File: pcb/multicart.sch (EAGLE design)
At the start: 15 parts, among them IC1 74HCT373N, IC2 M27C4001B, IC5 74HCT08N, Q1 BS170

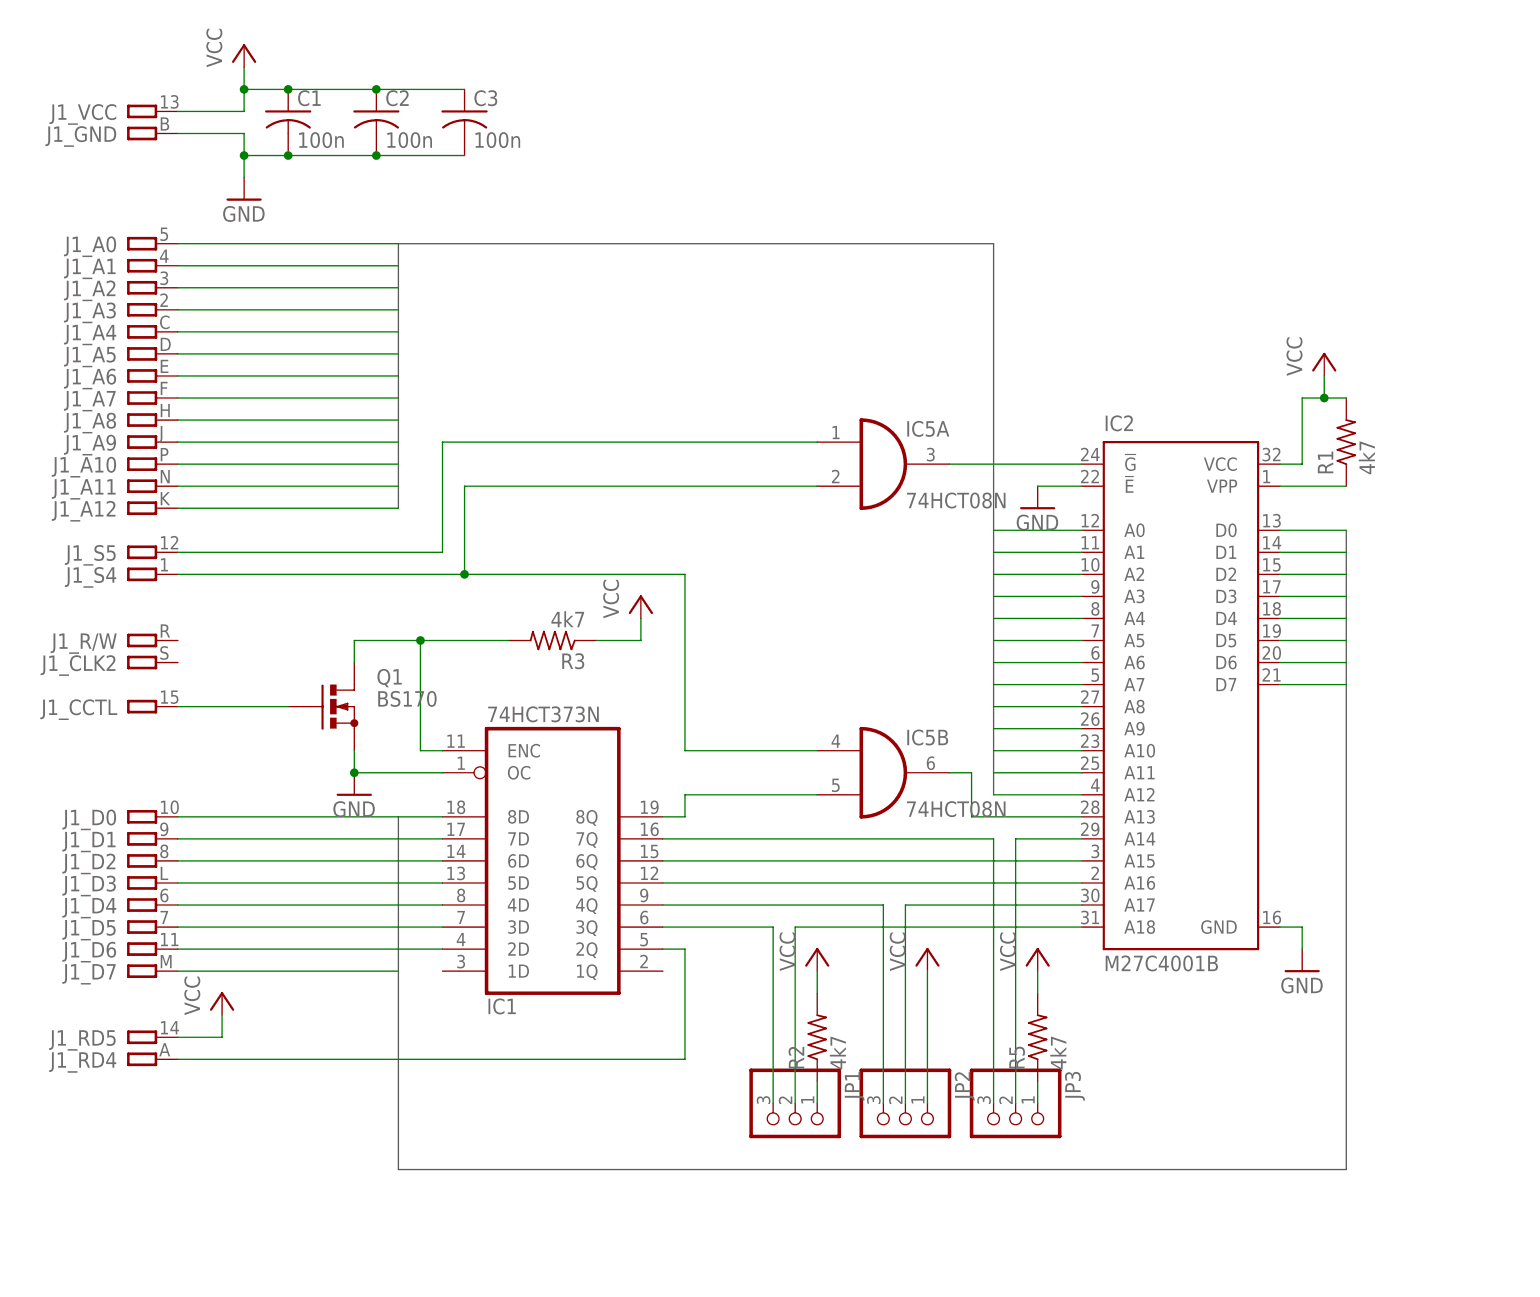
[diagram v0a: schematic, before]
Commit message: Updated the schematic to support 8-mbit flash chips.
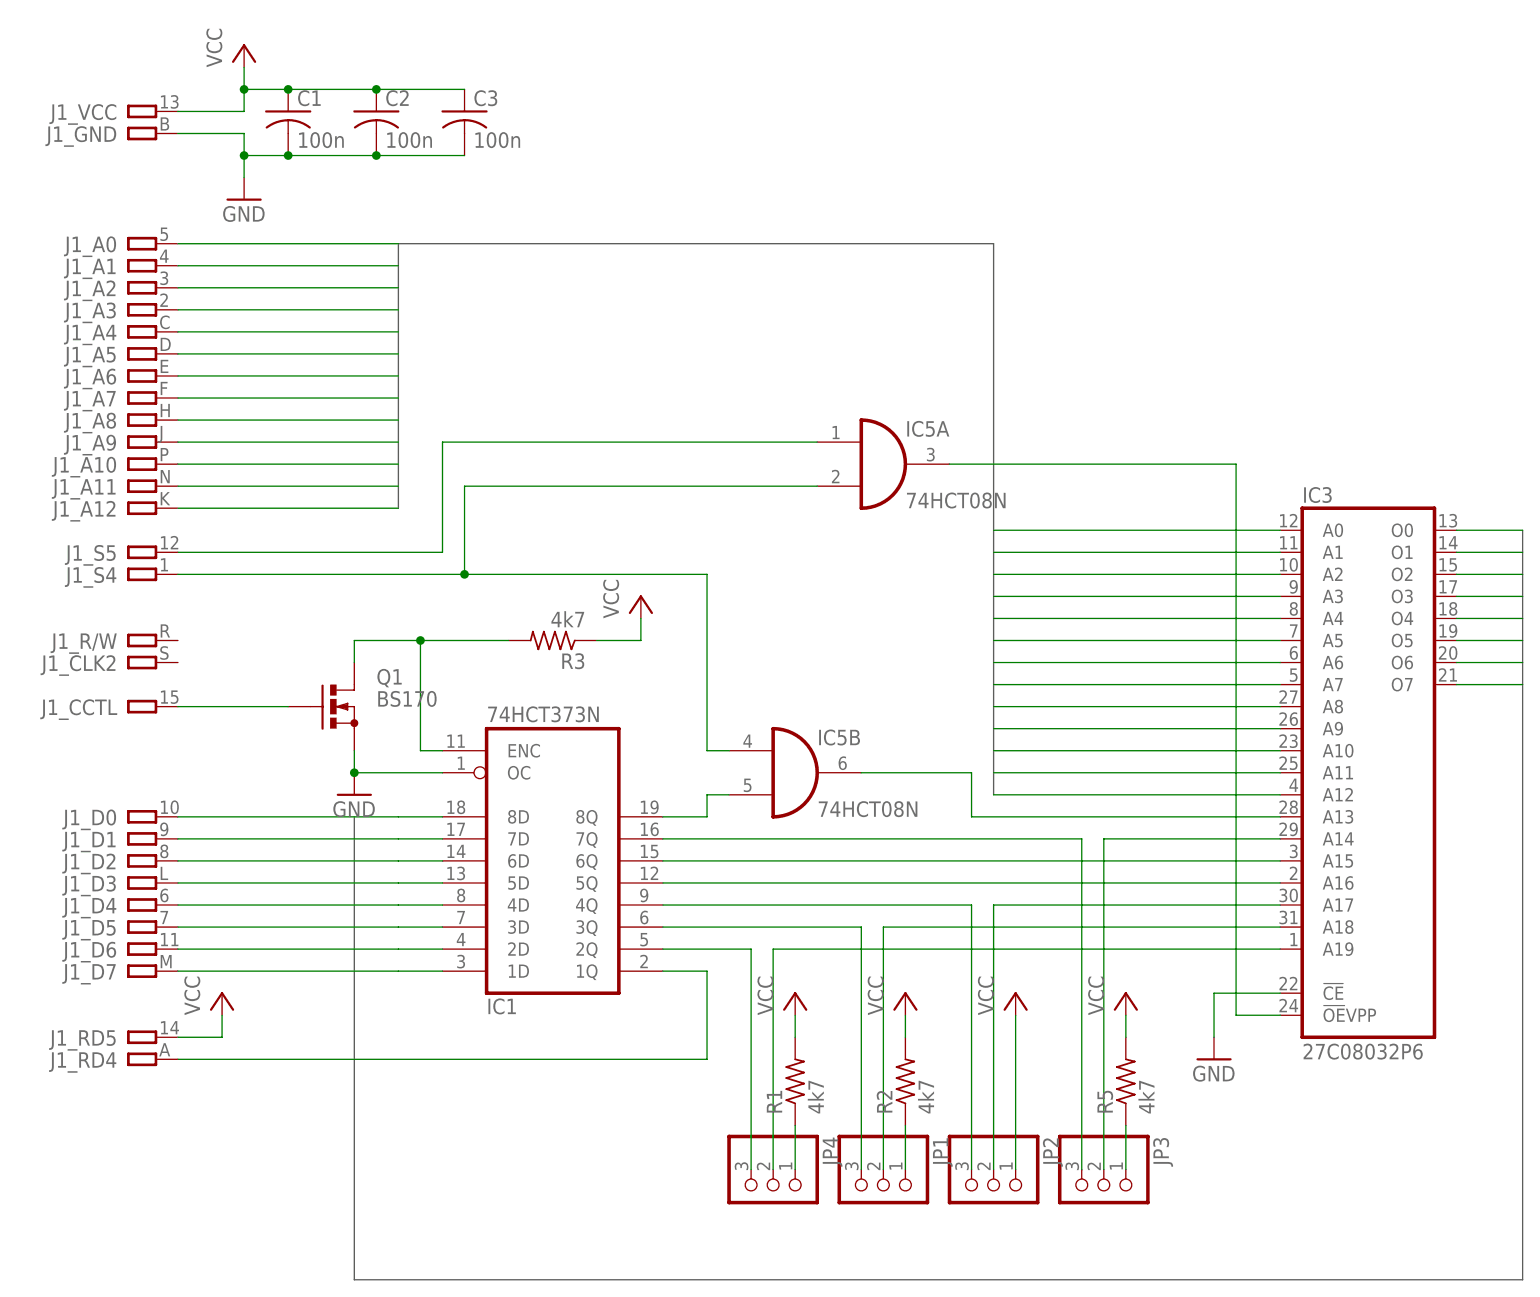
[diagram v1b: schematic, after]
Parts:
- removed IC2: M27C4001B, st-microelectronics:M27C4001B
- added IC3: 27C08032P6, atmel:27C08032P6
- added JP4: (no value), pinhead:PINHD-1X3
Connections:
- new net N$13: IC3G$1.A19, JP4.2
- new net N$14: IC1A.2Q, JP4.3
- net A0: now also IC3G$1.A0; no longer IC2.A0
- net A1: now also IC3G$1.A1; no longer IC2.A1
- net A10: now also IC3G$1.A10; no longer IC2.A10
- net A11: now also IC3G$1.A11; no longer IC2.A11
- net A12: now also IC3G$1.A12; no longer IC2.A12
- net A2: now also IC3G$1.A2; no longer IC2.A2
- net A3: now also IC3G$1.A3; no longer IC2.A3
- net A4: now also IC3G$1.A4; no longer IC2.A4
- net A5: now also IC3G$1.A5; no longer IC2.A5
- net A6: now also IC3G$1.A6; no longer IC2.A6
- net A7: now also IC3G$1.A7; no longer IC2.A7
- net A8: now also IC3G$1.A8; no longer IC2.A8
- net A9: now also IC3G$1.A9; no longer IC2.A9
- net D0: now also IC3G$1.O0; no longer IC2.D0
- net D1: now also IC3G$1.O1; no longer IC2.D1
- net D2: now also IC3G$1.O2; no longer IC2.D2
- net D3: now also IC3G$1.O3; no longer IC2.D3
- net D4: now also IC3G$1.O4; no longer IC2.D4
- net D5: now also IC3G$1.O5; no longer IC2.D5
- net D6: now also IC3G$1.O6; no longer IC2.D6
- net D7: now also IC1A.1D, IC3G$1.O7; no longer IC2.D7
- net GND: now also IC3G$1.!CE; no longer IC2.!E, IC2.GND
- net N$10: now also IC3G$1.A18; no longer IC2.A18
- net N$12: now also IC3G$1.A17; no longer IC2.A17
- net N$15: now also IC3G$1.A14; no longer IC2.A14
- net N$21: now also IC3G$1.A13; no longer IC2.A13
- net N$22: now also IC1A.1Q; no longer IC1A.2Q
- net N$27: now also IC3G$1.!OE!VPP; no longer IC2.!G
- net N$3: now also IC3G$1.A15; no longer IC2.A15
- net N$4: now also IC3G$1.A16; no longer IC2.A16
- net N$9: now also JP4.1; no longer IC2.VPP
- net VCC: no longer IC2.VCC
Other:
- moved on the sheet: IC5B, JP1, JP2, JP3, R1, R2, R5

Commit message: Updated the PCB design.
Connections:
- net N$10: now also JP2.2; no longer JP1.2
- net N$11: now also JP2.1; no longer JP1.1
- net N$12: now also JP3.2; no longer JP2.2
- net N$13: now also JP1.2; no longer JP4.2
- net N$14: now also JP1.3; no longer JP4.3
- net N$15: now also JP4.2; no longer JP3.2
- net N$16: now also JP4.1; no longer JP3.1
- net N$2: now also JP4.3; no longer JP3.3
- net N$5: now also JP3.3; no longer JP2.3
- net N$6: now also JP2.3; no longer JP1.3
- net N$9: now also JP1.1; no longer JP4.1
- net VCC: now also JP3.1; no longer JP2.1
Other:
- moved on the sheet: JP1, JP2, JP3, JP4
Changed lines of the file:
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@@
 <part name="R1" library="resistor" deviceset="R-US_" device="0204/7" value="4k7"/>
 <part name="R2" library="resistor" deviceset="R-US_" device="0204/7" value="4k7"/>
+<part name="JP3" library="pinhead" deviceset="PINHD-1X3" device=""/>
+<part name="P+5" library="supply1" deviceset="VCC" device=""/>
 <part name="JP2" library="pinhead" deviceset="PINHD-1X3" device=""/>
-<part name="P+5" library="supply1" deviceset="VCC" device=""/>
-<part name="JP1" library="pinhead" deviceset="PINHD-1X3" device=""/>
 <part name="P+3" library="supply1" deviceset="VCC" device=""/>
-<part name="JP3" library="pinhead" deviceset="PINHD-1X3" device=""/>
+<part name="JP4" library="pinhead" deviceset="PINHD-1X3" device=""/>
 <part name="R5" library="resistor" deviceset="R-US_" device="0204/7" value="4k7"/>
 <part name="P+6" library="supply1" deviceset="VCC" device=""/>
@@
 <part name="Q1" library="transistor-small-signal" deviceset="BS170" device=""/>
 <part name="IC3" library="atmel" deviceset="27C080" device="32P6"/>
-<part name="JP4" library="pinhead" deviceset="PINHD-1X3" device=""/>
+<part name="JP1" library="pinhead" deviceset="PINHD-1X3" device=""/>
 </parts>
 <sheets>
@@
 <instance part="R1" gate="G$1" x="68.58" y="17.78" rot="R90"/>
 <instance part="R2" gate="G$1" x="81.28" y="17.78" rot="R90"/>
-<instance part="JP2" gate="A" x="91.44" y="5.08" rot="R270"/>
+<instance part="JP3" gate="A" x="91.44" y="5.08" rot="R270"/>
 <instance part="P+5" gate="VCC" x="93.98" y="27.94"/>
-<instance part="JP1" gate="A" x="78.74" y="5.08" rot="R270"/>
+<instance part="JP2" gate="A" x="78.74" y="5.08" rot="R270"/>
 <instance part="P+3" gate="VCC" x="81.28" y="27.94"/>
-<instance part="JP3" gate="A" x="104.14" y="5.08" rot="R270"/>
+<instance part="JP4" gate="A" x="104.14" y="5.08" rot="R270"/>
 <instance part="R5" gate="G$1" x="106.68" y="17.78" rot="R90"/>
 <instance part="P+6" gate="VCC" x="106.68" y="27.94"/>
@@
 <instance part="Q1" gate="1" x="15.24" y="60.96"/>
 <instance part="IC3" gate="G$1" x="134.62" y="53.34"/>
-<instance part="JP4" gate="A" x="66.04" y="5.08" rot="R270"/>
+<instance part="JP1" gate="A" x="66.04" y="5.08" rot="R270"/>
 </instances>
 <busses>
@@
 <segment>
 <pinref part="J1" gate="_D0" pin="P"/>
-<wire x1="-2.54" y1="48.26" x2="22.86" y2="48.26" width="0.1524" layer="91"/>
+<wire x1="-2.54" y1="48.26" x2="17.78" y2="48.26" width="0.1524" layer="91"/>
 </segment>
 <segment>
 <pinref part="IC1" gate="A" pin="8D"/>
-<wire x1="22.86" y1="48.26" x2="27.94" y2="48.26" width="0.1524" layer="91"/>
+<wire x1="17.78" y1="48.26" x2="27.94" y2="48.26" width="0.1524" layer="91"/>
 </segment>
 <segment>
@@
 <segment>
 <pinref part="J1" gate="_D1" pin="P"/>
-<wire x1="-2.54" y1="45.72" x2="22.86" y2="45.72" width="0.1524" layer="91"/>
+<wire x1="-2.54" y1="45.72" x2="17.78" y2="45.72" width="0.1524" layer="91"/>
 </segment>
 <segment>
 <pinref part="IC1" gate="A" pin="7D"/>
-<wire x1="22.86" y1="45.72" x2="27.94" y2="45.72" width="0.1524" layer="91"/>
+<wire x1="17.78" y1="45.72" x2="27.94" y2="45.72" width="0.1524" layer="91"/>
 </segment>
 <segment>
@@
 <segment>
 <pinref part="J1" gate="_D2" pin="P"/>
-<wire x1="-2.54" y1="43.18" x2="22.86" y2="43.18" width="0.1524" layer="91"/>
+<wire x1="-2.54" y1="43.18" x2="17.78" y2="43.18" width="0.1524" layer="91"/>
 </segment>
 <segment>
 <pinref part="IC1" gate="A" pin="6D"/>
-<wire x1="22.86" y1="43.18" x2="27.94" y2="43.18" width="0.1524" layer="91"/>
+<wire x1="17.78" y1="43.18" x2="27.94" y2="43.18" width="0.1524" layer="91"/>
 </segment>
 <segment>
@@
 <segment>
 <pinref part="J1" gate="_D3" pin="P"/>
-<wire x1="-2.54" y1="40.64" x2="22.86" y2="40.64" width="0.1524" layer="91"/>
+<wire x1="-2.54" y1="40.64" x2="17.78" y2="40.64" width="0.1524" layer="91"/>
 </segment>
 <segment>
 <pinref part="IC1" gate="A" pin="5D"/>
-<wire x1="22.86" y1="40.64" x2="27.94" y2="40.64" width="0.1524" layer="91"/>
+<wire x1="17.78" y1="40.64" x2="27.94" y2="40.64" width="0.1524" layer="91"/>
 </segment>
 <segment>
@@
 <segment>
 <pinref part="J1" gate="_D4" pin="P"/>
-<wire x1="-2.54" y1="38.1" x2="22.86" y2="38.1" width="0.1524" layer="91"/>
+<wire x1="-2.54" y1="38.1" x2="17.78" y2="38.1" width="0.1524" layer="91"/>
 </segment>
 <segment>
 <pinref part="IC1" gate="A" pin="4D"/>
-<wire x1="22.86" y1="38.1" x2="27.94" y2="38.1" width="0.1524" layer="91"/>
+<wire x1="17.78" y1="38.1" x2="27.94" y2="38.1" width="0.1524" layer="91"/>
 </segment>
 <segment>
@@
 <segment>
 <pinref part="J1" gate="_D5" pin="P"/>
-<wire x1="-2.54" y1="35.56" x2="22.86" y2="35.56" width="0.1524" layer="91"/>
+<wire x1="-2.54" y1="35.56" x2="17.78" y2="35.56" width="0.1524" layer="91"/>
 </segment>
 <segment>
 <pinref part="IC1" gate="A" pin="3D"/>
-<wire x1="22.86" y1="35.56" x2="27.94" y2="35.56" width="0.1524" layer="91"/>
+<wire x1="17.78" y1="35.56" x2="27.94" y2="35.56" width="0.1524" layer="91"/>
 </segment>
 <segment>
@@
 <segment>
 <pinref part="J1" gate="_D6" pin="P"/>
-<wire x1="-2.54" y1="33.02" x2="22.86" y2="33.02" width="0.1524" layer="91"/>
+<wire x1="-2.54" y1="33.02" x2="17.78" y2="33.02" width="0.1524" layer="91"/>
 </segment>
 <segment>
@@
 <segment>
 <pinref part="IC1" gate="A" pin="2D"/>
-<wire x1="22.86" y1="33.02" x2="27.94" y2="33.02" width="0.1524" layer="91"/>
+<wire x1="17.78" y1="33.02" x2="27.94" y2="33.02" width="0.1524" layer="91"/>
 </segment>
 </net>
@@
 <segment>
 <pinref part="J1" gate="_D7" pin="P"/>
-<wire x1="-2.54" y1="30.48" x2="22.86" y2="30.48" width="0.1524" layer="91"/>
+<wire x1="-2.54" y1="30.48" x2="17.78" y2="30.48" width="0.1524" layer="91"/>
 </segment>
 <segment>
@@
 <segment>
 <pinref part="IC1" gate="A" pin="1D"/>
-<wire x1="22.86" y1="30.48" x2="27.94" y2="30.48" width="0.1524" layer="91"/>
+<wire x1="17.78" y1="30.48" x2="27.94" y2="30.48" width="0.1524" layer="91"/>
 </segment>
 </net>
@@
 <segment>
 <pinref part="P+5" gate="VCC" pin="VCC"/>
-<pinref part="JP2" gate="A" pin="1"/>
+<pinref part="JP3" gate="A" pin="1"/>
 <wire x1="93.98" y1="25.4" x2="93.98" y2="7.62" width="0.1524" layer="91"/>
 </segment>
@@
 <pinref part="IC1" gate="A" pin="4Q"/>
 <wire x1="53.34" y1="38.1" x2="88.9" y2="38.1" width="0.1524" layer="91"/>
-<pinref part="JP2" gate="A" pin="3"/>
+<pinref part="JP3" gate="A" pin="3"/>
 <wire x1="88.9" y1="38.1" x2="88.9" y2="7.62" width="0.1524" layer="91"/>
 </segment>
@@
 <segment>
 <wire x1="91.44" y1="38.1" x2="124.46" y2="38.1" width="0.1524" layer="91"/>
-<pinref part="JP2" gate="A" pin="2"/>
+<pinref part="JP3" gate="A" pin="2"/>
 <wire x1="91.44" y1="38.1" x2="91.44" y2="7.62" width="0.1524" layer="91"/>
 <pinref part="IC3" gate="G$1" pin="A17"/>
@@
 <segment>
 <pinref part="IC1" gate="A" pin="3Q"/>
-<pinref part="JP1" gate="A" pin="3"/>
+<pinref part="JP2" gate="A" pin="3"/>
 <wire x1="53.34" y1="35.56" x2="76.2" y2="35.56" width="0.1524" layer="91"/>
 <wire x1="76.2" y1="35.56" x2="76.2" y2="7.62" width="0.1524" layer="91"/>
@@
 <net name="N$10" class="0">
 <segment>
-<pinref part="JP1" gate="A" pin="2"/>
+<pinref part="JP2" gate="A" pin="2"/>
 <wire x1="124.46" y1="35.56" x2="78.74" y2="35.56" width="0.1524" layer="91"/>
 <wire x1="78.74" y1="35.56" x2="78.74" y2="7.62" width="0.1524" layer="91"/>
@@
 <net name="N$11" class="0">
 <segment>
-<pinref part="JP1" gate="A" pin="1"/>
+<pinref part="JP2" gate="A" pin="1"/>
 <pinref part="R2" gate="G$1" pin="1"/>
 <wire x1="81.28" y1="7.62" x2="81.28" y2="12.7" width="0.1524" layer="91"/>
@@
 <segment>
 <pinref part="IC1" gate="A" pin="7Q"/>
-<pinref part="JP3" gate="A" pin="3"/>
+<pinref part="JP4" gate="A" pin="3"/>
 <wire x1="53.34" y1="45.72" x2="101.6" y2="45.72" width="0.1524" layer="91"/>
 <wire x1="101.6" y1="45.72" x2="101.6" y2="7.62" width="0.1524" layer="91"/>
@@
 <net name="N$15" class="0">
 <segment>
-<pinref part="JP3" gate="A" pin="2"/>
+<pinref part="JP4" gate="A" pin="2"/>
 <wire x1="104.14" y1="7.62" x2="104.14" y2="45.72" width="0.1524" layer="91"/>
 <wire x1="104.14" y1="45.72" x2="124.46" y2="45.72" width="0.1524" layer="91"/>
@@
 <net name="N$16" class="0">
 <segment>
-<pinref part="JP3" gate="A" pin="1"/>
+<pinref part="JP4" gate="A" pin="1"/>
 <pinref part="R5" gate="G$1" pin="1"/>
 <wire x1="106.68" y1="7.62" x2="106.68" y2="12.7" width="0.1524" layer="91"/>
@@
 <segment>
 <pinref part="R1" gate="G$1" pin="1"/>
-<pinref part="JP4" gate="A" pin="1"/>
+<pinref part="JP1" gate="A" pin="1"/>
 <wire x1="68.58" y1="12.7" x2="68.58" y2="7.62" width="0.1524" layer="91"/>
 </segment>
@@
 <segment>
 <pinref part="IC3" gate="G$1" pin="A19"/>
-<pinref part="JP4" gate="A" pin="2"/>
+<pinref part="JP1" gate="A" pin="2"/>
 <wire x1="124.46" y1="33.02" x2="66.04" y2="33.02" width="0.1524" layer="91"/>
 <wire x1="66.04" y1="33.02" x2="66.04" y2="7.62" width="0.1524" layer="91"/>
@@
 <net name="N$14" class="0">
 <segment>
-<pinref part="JP4" gate="A" pin="3"/>
+<pinref part="JP1" gate="A" pin="3"/>
 <wire x1="63.5" y1="7.62" x2="63.5" y2="33.02" width="0.1524" layer="91"/>
 <pinref part="IC1" gate="A" pin="2Q"/>
